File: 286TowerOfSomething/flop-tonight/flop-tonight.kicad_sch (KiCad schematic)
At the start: 1 part, among them J1 Bus_ISA_16bit

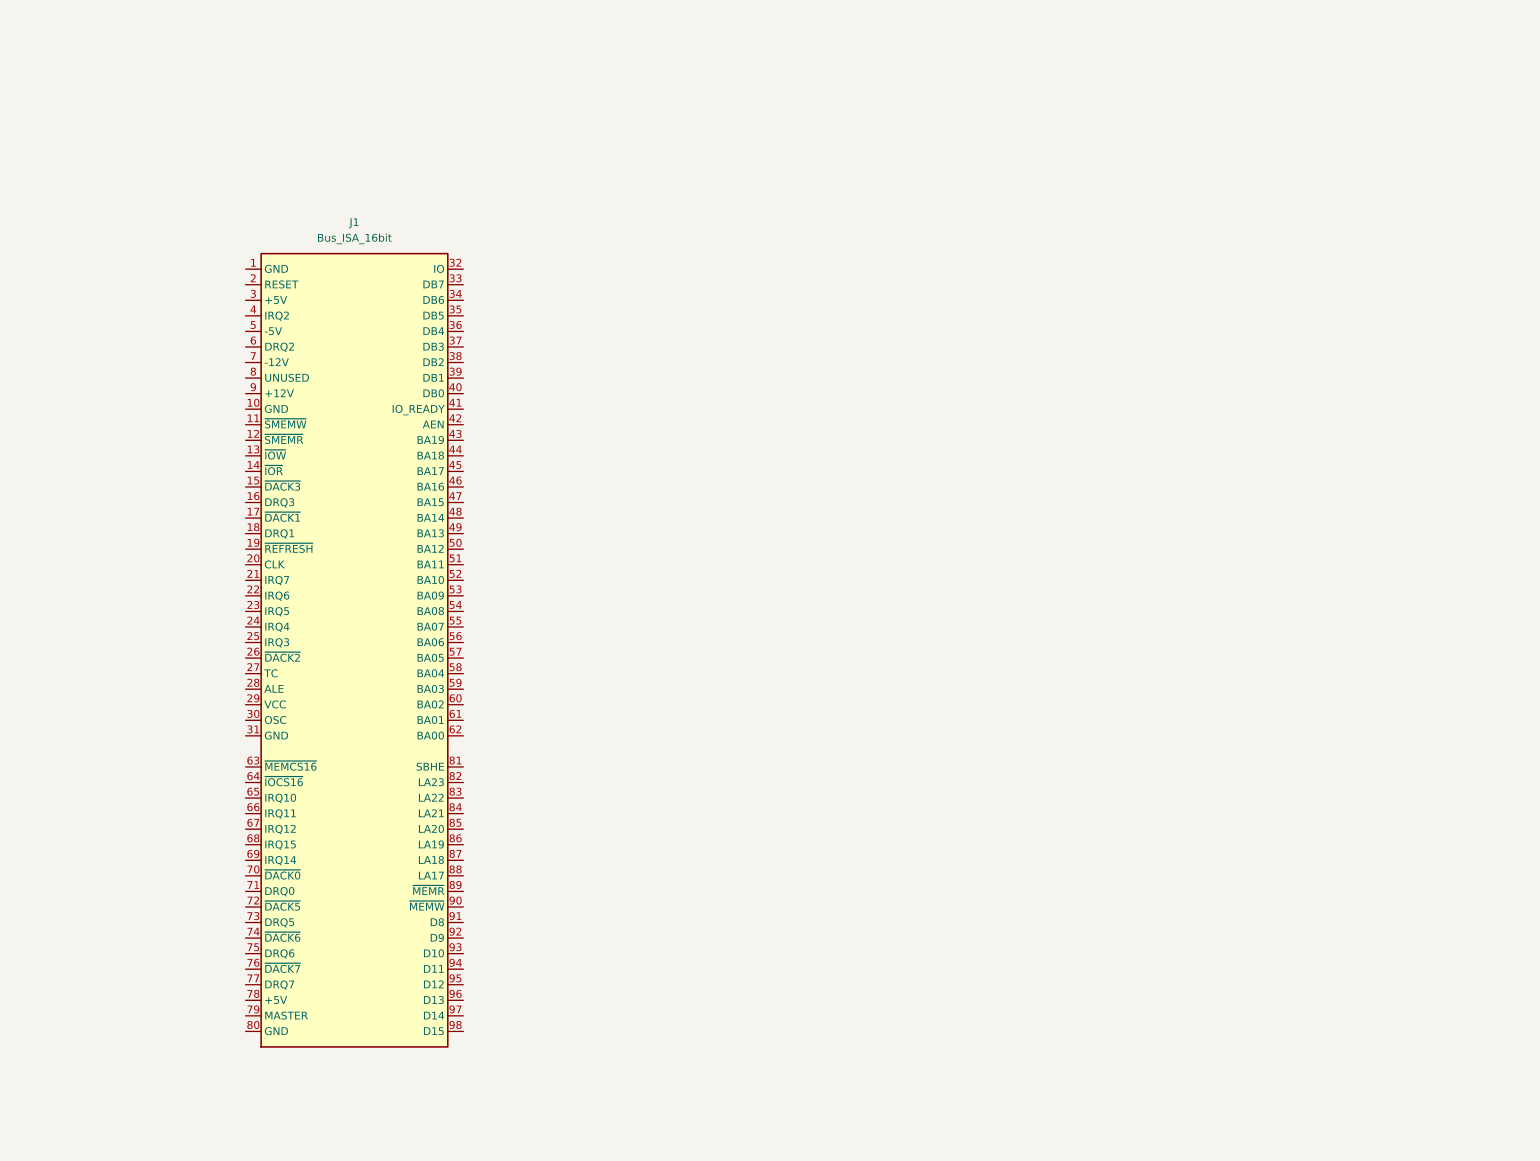
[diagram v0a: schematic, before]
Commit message: Started adding custom symbols and footprints. Schematic basically complete for flop-tonight
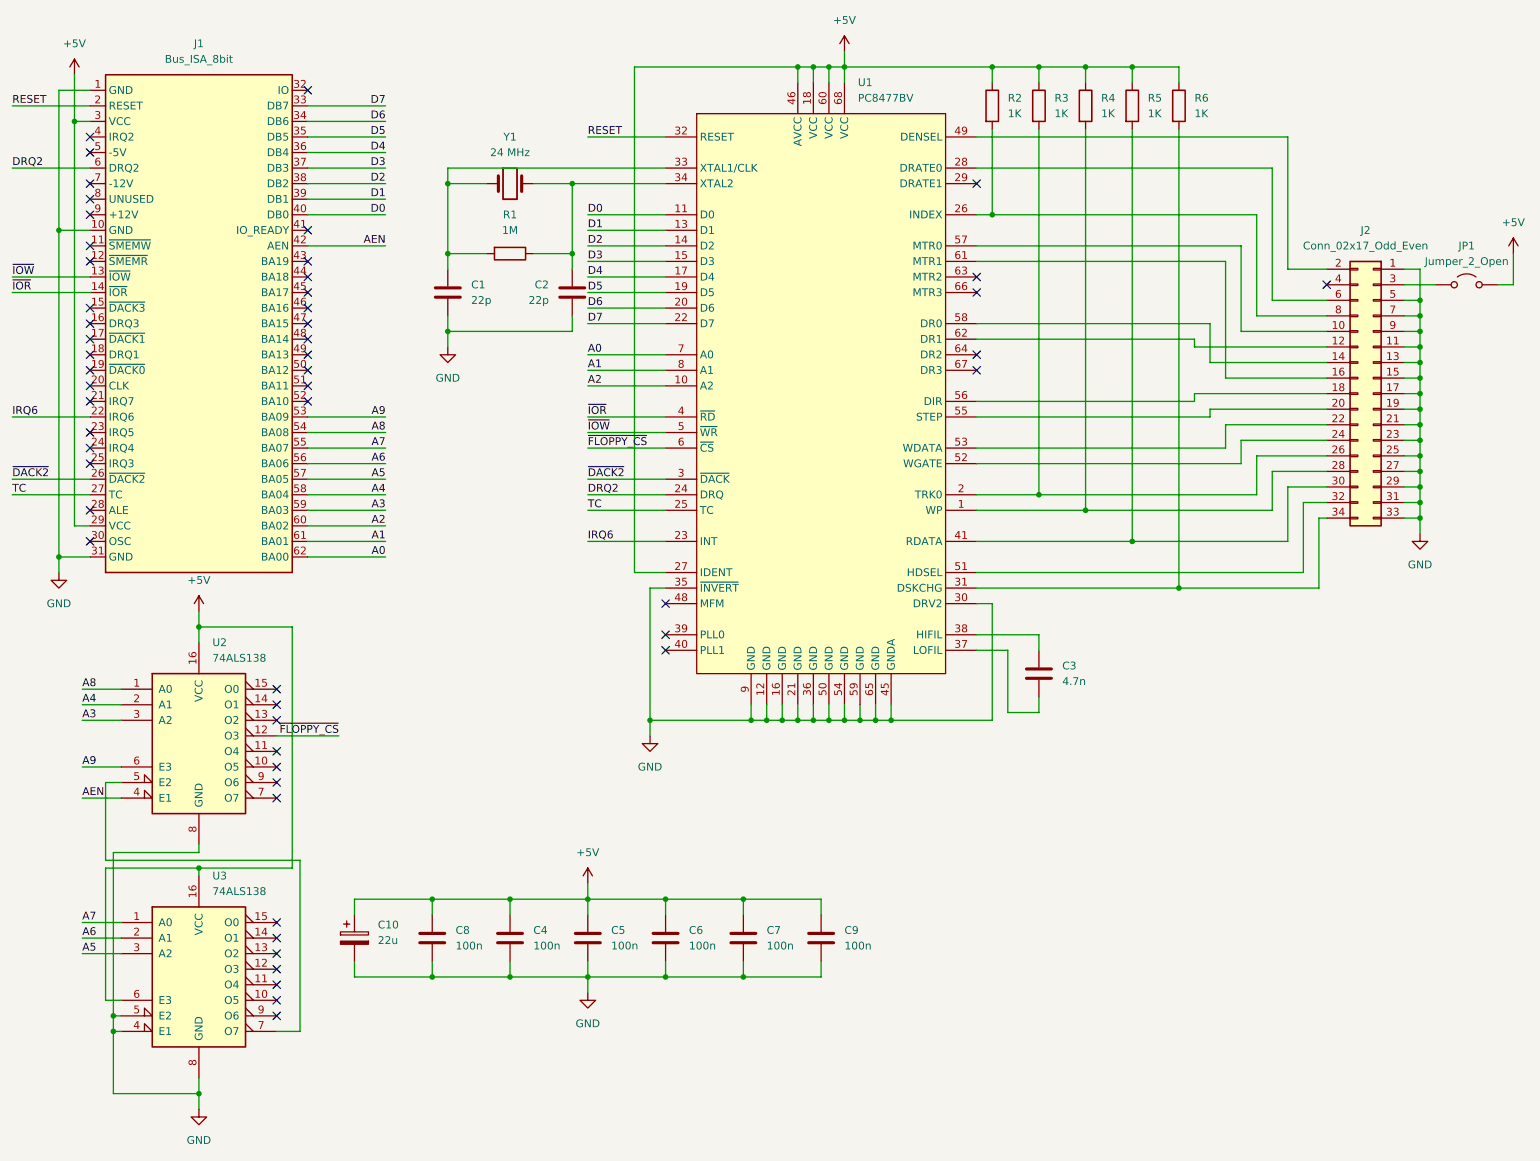
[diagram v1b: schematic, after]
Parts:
- removed J1: Bus_ISA_16bit, symbol Connector:Bus_ISA_16bit
- added C1, C2: 22p, Capacitor_SMD:C_0603_1608Metric_Pad1.08x0.95mm_HandSolder, symbol Device:C
- added C10: 22u, Capacitor_SMD:CP_Elec_5x5.3, symbol Device:C_Polarized
- added C3: 4.7n, Capacitor_SMD:C_0603_1608Metric_Pad1.08x0.95mm_HandSolder, symbol Device:C
- added C4, C5, C6, C7, C8, C9: 100n, Capacitor_SMD:C_0603_1608Metric_Pad1.08x0.95mm_HandSolder, symbol Device:C
- added J1: Bus_ISA_8bit, pc-parts:BUS_AT_8BIT, symbol Connector:Bus_ISA_8bit
- added J2: Conn_02x17_Odd_Even, Connector_IDC:IDC-Header_2x17_P2.54mm_Vertical, symbol Connector_Generic:Conn_02x17_Odd_Even
- added JP1: Jumper_2_Open, Connector_PinHeader_2.54mm:PinHeader_1x02_P2.54mm_Vertical, symbol Jumper:Jumper_2_Open
- added R1: 1M, Resistor_SMD:R_0603_1608Metric_Pad0.98x0.95mm_HandSolder, symbol Device:R
- added R2, R3, R4, R5, R6: 1K, Resistor_SMD:R_0603_1608Metric_Pad0.98x0.95mm_HandSolder, symbol Device:R
- added U1: PC8477BV, Package_LCC:PLCC-68_THT-Socket, symbol pc-parts:PC8477
- added U2, U3: 74ALS138, Package_DIP:DIP-16_W7.62mm, symbol 74xx:74LS138
- added Y1: 24 MHz, Crystal:Crystal_HC49-U_Vertical, symbol Device:Crystal
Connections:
- new net: J2.10 (Pin_10), U1.57 (MTR0)
- new net: J2.12 (Pin_12), U1.62 (DR1)
- new net: J2.14 (Pin_14), U1.58 (DR0)
- new net: J2.16 (Pin_16), U1.61 (MTR1)
- new net: J2.18 (Pin_18), U1.56 (DIR)
- new net: J2.2 (Pin_2), U1.49 (DENSEL)
- new net: J2.20 (Pin_20), U1.55 (STEP)
- new net: J2.22 (Pin_22), U1.53 (WDATA)
- new net: J2.24 (Pin_24), U1.52 (WGATE)
- new net: J2.26 (Pin_26), R3.2, U1.2 (TRK0)
- new net: J2.28 (Pin_28), R4.2, U1.1 (WP)
- new net: J2.3 (Pin_3), JP1.1 (A)
- new net: J2.30 (Pin_30), R5.2, U1.41 (RDATA)
- new net: J2.32 (Pin_32), U1.51 (HDSEL)
- new net: J2.34 (Pin_34), R6.2, U1.31 (DSKCHG)
- new net: J2.6 (Pin_6), U1.28 (DRATE0)
- new net: J2.8 (Pin_8), R2.2, U1.26 (INDEX)
- new net: C2.1, R1.1, U1.34 (XTAL2), Y1.2
- new net: C1.1, R1.2, U1.33 (XTAL1/CLK), Y1.1
- new net: U2.5 (E2), U3.7 (O7)
- new net: C3.1, U1.38 (HIFIL)
- new net: C3.2, U1.37 (LOFIL)
- new net +5V: C10.1, C4.1, C5.1, C6.1, C7.1, C8.1, C9.1, J1.29 (VCC), J1.3 (VCC), JP1.2 (B), R2.1, R3.1, R4.1, R5.1, R6.1, U1.18 (VCC), U1.27 (IDENT), U1.46 (AVCC), U1.60 (VCC), U1.68 (VCC), U2.16 (VCC), U3.16 (VCC), U3.6 (E3)
- new net A0: J1.62 (BA00), U1.7 (A0)
- new net A1: J1.61 (BA01), U1.8 (A1)
- new net A2: J1.60 (BA02), U1.10 (A2)
- new net A3: J1.59 (BA03), U2.3 (A2)
- new net A4: J1.58 (BA04), U2.2 (A1)
- new net A5: J1.57 (BA05), U3.3 (A2)
- new net A6: J1.56 (BA06), U3.2 (A1)
- new net A7: J1.55 (BA07), U3.1 (A0)
- new net A8: J1.54 (BA08), U2.1 (A0)
- new net A9: J1.53 (BA09), U2.6 (E3)
- new net AEN: J1.42 (AEN), U2.4 (E1)
- new net D0: J1.40 (DB0), U1.11 (D0)
- new net D1: J1.39 (DB1), U1.13 (D1)
- new net D2: J1.38 (DB2), U1.14 (D2)
- new net D3: J1.37 (DB3), U1.15 (D3)
- new net D4: J1.36 (DB4), U1.17 (D4)
- new net D5: J1.35 (DB5), U1.19 (D5)
- new net D6: J1.34 (DB6), U1.20 (D6)
- new net D7: J1.33 (DB7), U1.22 (D7)
- new net DRQ2: J1.6 (DRQ2), U1.24 (DRQ)
- new net GND: C1.2, C10.2, C2.2, C4.2, C5.2, C6.2, C7.2, C8.2, C9.2, J1.1 (GND), J1.10 (GND), J1.31 (GND), J2.1 (Pin_1), J2.11 (Pin_11), J2.13 (Pin_13), J2.15 (Pin_15), J2.17 (Pin_17), J2.19 (Pin_19), J2.21 (Pin_21), J2.23 (Pin_23), J2.25 (Pin_25), J2.27 (Pin_27), J2.29 (Pin_29), J2.31 (Pin_31), J2.33 (Pin_33), J2.5 (Pin_5), J2.7 (Pin_7), J2.9 (Pin_9), U1.12 (GND), U1.16 (GND), U1.21 (GND), U1.30 (DRV2), U1.35 (~{INVERT}), U1.36 (GND), U1.45 (GNDA), U1.50 (GND), U1.54 (GND), U1.59 (GND), U1.65 (GND), U1.9 (GND), U2.8 (GND), U3.4 (E1), U3.5 (E2), U3.8 (GND)
- new net IRQ6: J1.22 (IRQ6), U1.23 (INT)
- new net RESET: J1.2 (RESET), U1.32 (RESET)
- new net TC: J1.27 (TC), U1.25 (TC)
- new net ~{DACK2}: J1.26 (~{DACK2}), U1.3 (~{DACK})
- new net ~{FLOPPY_CS}: U1.6 (~{CS}), U2.12 (O3)
- new net ~{IOR}: J1.14 (~{IOR}), U1.4 (~{RD})
- new net ~{IOW}: J1.13 (~{IOW}), U1.5 (~{WR})
- no-connect marks 0 -> 54
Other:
- company: (none) -> Surreality Labs
- title: (none) -> Flop Tonight
